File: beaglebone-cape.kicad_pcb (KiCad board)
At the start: 2 copper layers, 86.4 x 54.6 mm, 9 parts, among them J1 CONN_2X2, P1 BEAGLEBONE_BLACK, U1 24C16

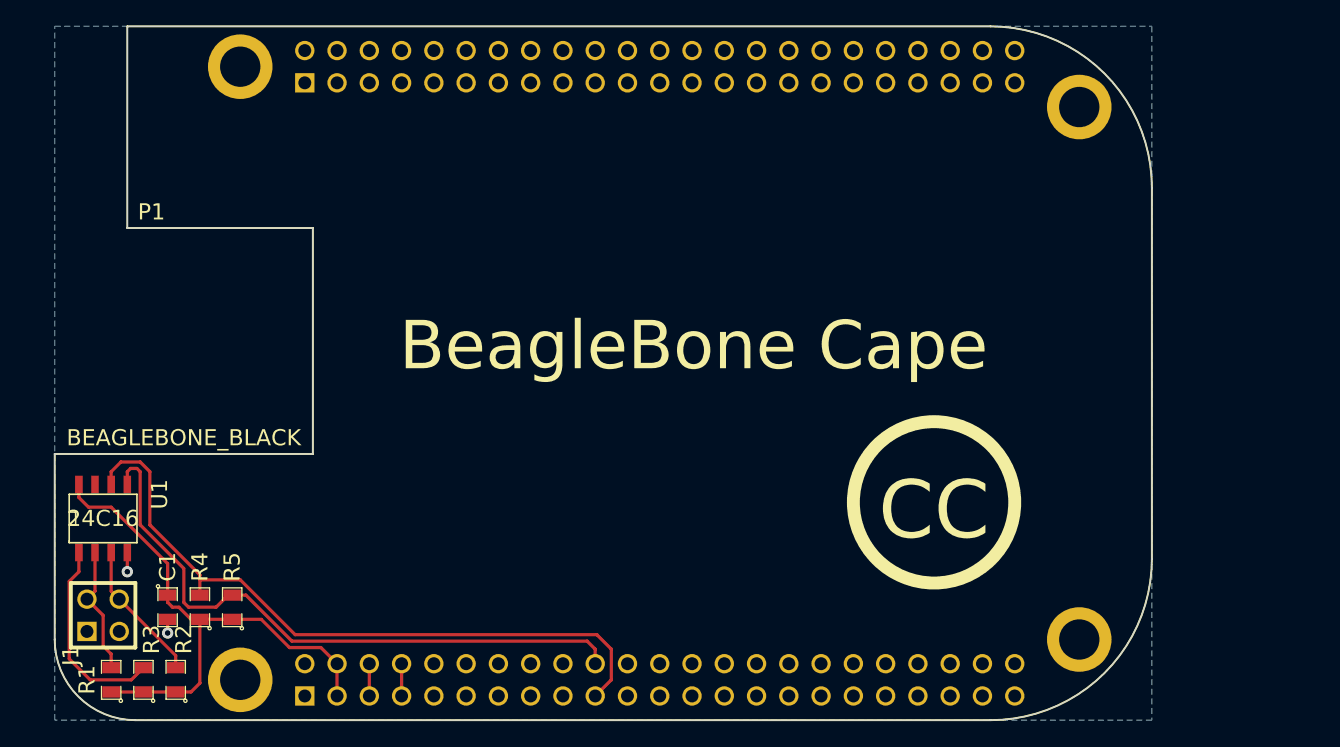
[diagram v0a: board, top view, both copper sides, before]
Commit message: Create the io cape base on the barebone cape
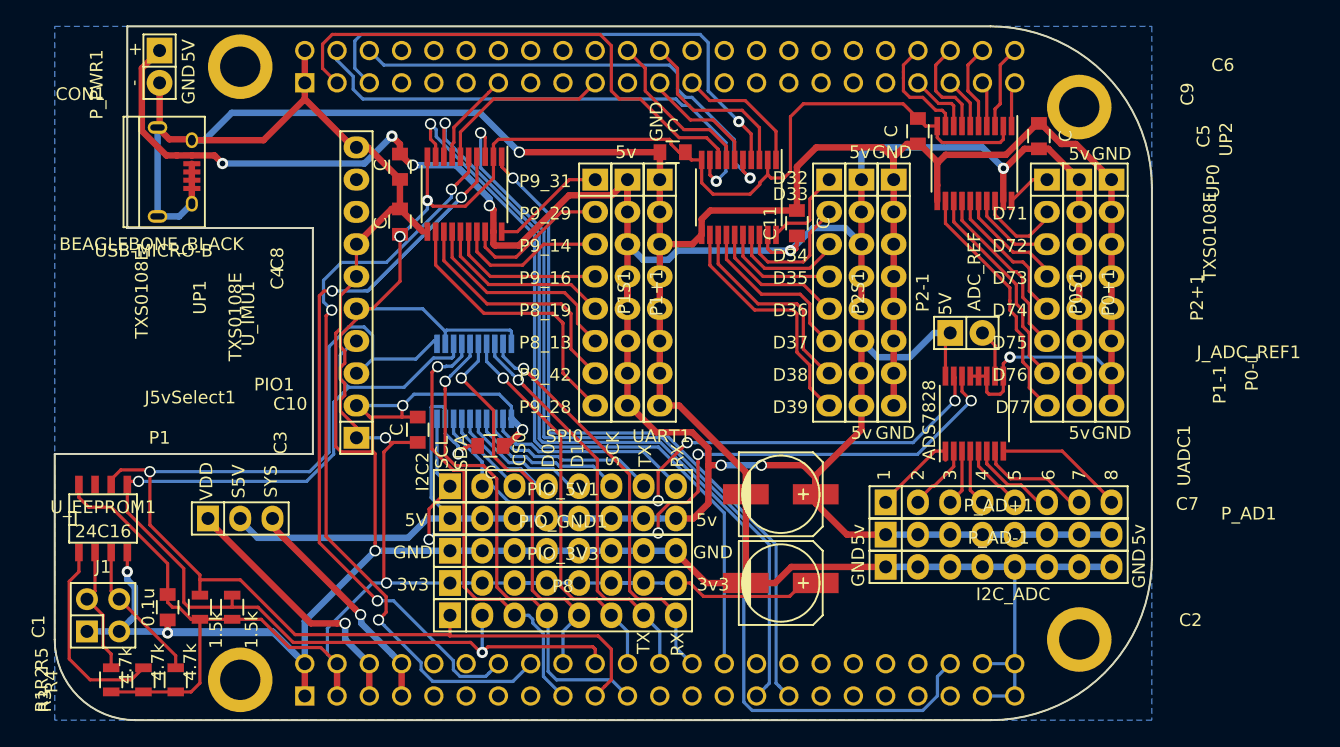
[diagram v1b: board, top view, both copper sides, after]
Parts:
- removed U1: 24C16, SO8E
- added C10: C, Capacitors_SMD:C_0805, F.Cu at (130.8, 118.1)
- added C11: C, Capacitors_SMD:C_0805, F.Cu at (154.9, 100.6)
- added C2: CP2, Capacitors_SMD:c_elec_6.3x5.7, F.Cu at (153.7, 128.9)
- added C3: C, Capacitors_SMD:C_0805, F.Cu at (125.1, 116.8)
- added C4: C, Capacitors_SMD:C_0805, F.Cu at (123.7, 100.5)
- added C5: C, Capacitors_SMD:C_0805, F.Cu at (164.5, 93.3)
- added C6: C, Capacitors_SMD:C_0805, F.Cu at (145.2, 95.0)
- added C7: CP2, Capacitors_SMD:c_elec_6.3x5.7, F.Cu at (153.7, 121.9)
- added C8: C, Capacitors_SMD:C_0805, F.Cu at (123.7, 96.1)
- added C9: C, Capacitors_SMD:C_0805, F.Cu at (174.0, 93.7)
- added CON1: USB-MICRO-B, Connect:USB_Micro-B, F.Cu at (107.3, 95.2)
- added J5vSelect1: CONN_01X03, Pin_Headers:Pin_Header_Straight_1x03, F.Cu at (111.1, 123.8)
- added J_ADC_REF1: CONN_01X02, Pin_Headers:Pin_Header_Straight_1x02, F.Cu at (168.3, 109.2)
- added P0+1: CONN_01X08, Pin_Headers:Pin_Header_Straight_1x08, F.Cu at (177.2, 106.0)
- added P0-1: CONN_01X08, Pin_Headers:Pin_Header_Straight_1x08, F.Cu at (179.7, 106.0)
- added P0S1: CONN_01X08, Pin_Headers:Pin_Header_Straight_1x08, F.Cu at (174.6, 106.0)
- added P1+1: CONN_01X08, Pin_Headers:Pin_Header_Straight_1x08, F.Cu at (141.6, 106.0)
- added P1-1: CONN_01X08, Pin_Headers:Pin_Header_Straight_1x08, F.Cu at (144.1, 106.0)
- added P1S1: CONN_01X08, Pin_Headers:Pin_Header_Straight_1x08, F.Cu at (139.1, 106.0)
- added P2+1: CONN_01X08, Pin_Headers:Pin_Header_Straight_1x08, F.Cu at (160.0, 106.0)
- added P2-1: CONN_01X08, Pin_Headers:Pin_Header_Straight_1x08, F.Cu at (162.6, 106.0)
- added P2S1: CONN_01X08, Pin_Headers:Pin_Header_Straight_1x08, F.Cu at (157.5, 106.0)
- added P8: CONN_01X08, Pin_Headers:Pin_Header_Straight_1x08, F.Cu at (136.5, 131.4)
- added PIO1: CONN_01X08, Pin_Headers:Pin_Header_Straight_1x08, F.Cu at (136.5, 121.3)
- added PIO_3V3: CONN_01X08, Pin_Headers:Pin_Header_Straight_1x08, F.Cu at (136.5, 128.9)
- added PIO_5V1: CONN_01X08, Pin_Headers:Pin_Header_Straight_1x08, F.Cu at (136.5, 123.8)
- added PIO_GND1: CONN_01X08, Pin_Headers:Pin_Header_Straight_1x08, F.Cu at (136.5, 126.4)
- added P_AD+1: CONN_01X08, Pin_Headers:Pin_Header_Straight_1x08, F.Cu at (170.8, 125.1)
- added P_AD-1: CONN_01X08, Pin_Headers:Pin_Header_Straight_1x08, F.Cu at (170.8, 127.6)
- added P_AD1: CONN_01X08, Pin_Headers:Pin_Header_Straight_1x08, F.Cu at (170.8, 122.6)
- added P_PWR1: CONN_01X02, Pin_Headers:Pin_Header_Straight_1x02, F.Cu at (104.8, 88.3)
- added UADC1: ADS7828, Housings_SSOP:TSSOP-16_4.4x5mm_Pitch0.65mm, F.Cu at (168.9, 115.6)
- added UP0: TXS0108E, Housings_SSOP:TSSOP-20_4.4x6.5mm_Pitch0.65mm, F.Cu at (168.9, 95.9)
- added UP1: TXS0108E, Housings_SSOP:TSSOP-20_4.4x6.5mm_Pitch0.65mm, F.Cu at (128.8, 98.3)
- added UP2: TXS0108E, Housings_SSOP:TSSOP-20_4.4x6.5mm_Pitch0.65mm, F.Cu at (150.4, 98.6)
- added UPIO1: TXS0108E, Housings_SSOP:TSSOP-20_4.4x6.5mm_Pitch0.65mm, B.Cu at (129.5, 113.0)
- added U_EEPROM1: 24C16, SMD_Packages:SOIC-8-W, F.Cu at (100.3, 123.8)
- added U_IMU1: BMX055-Breakout, Pin_Headers:Pin_Header_Straight_1x10, F.Cu at (120.3, 106.0)
- C1: footprint SM0805 -> Capacitors_SMD:C_0805
- J1: value CONN_2X2 -> CONN_02X02; footprint PIN_ARRAY_2X2 -> Pin_Headers:Pin_Header_Straight_2x02
- P1: footprint BEAGLEBONE_BLACK -> BeagleBoneBlack Cape:BEAGLEBONE_BLACK
- R1, R2, R3, R4, R5: footprint SM0805 -> Resistors_SMD:R_0805
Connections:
- P1 pad A10: (no net) -> /TIMER6
- P1 pad A11: (no net) -> /GPIO1_13
- P1 pad A12: (no net) -> /GPIO1_12
- P1 pad A13: (no net) -> /EHRPWM2B
- P1 pad A14: (no net) -> /GPIO0_26
- P1 pad A15: (no net) -> /GPIO1_15
- P1 pad A16: (no net) -> /GPIO1_14
- P1 pad A17: (no net) -> /GPIO0_27
- P1 pad A18: (no net) -> /GPIO2_1
- P1 pad A19: (no net) -> /EHRPWM2A
- P1 pad A20: (no net) -> /GPIO1_31
- P1 pad A21: (no net) -> /GPIO1_30
- P1 pad A22: (no net) -> /GPIO1_5
- P1 pad A23: (no net) -> /GPIO1_4
- P1 pad A24: (no net) -> /GPIO1_1
- P1 pad A25: (no net) -> /GPIO1_0
- P1 pad A26: (no net) -> /GPIO1_29
- P1 pad A27: (no net) -> /GPIO2_22
- P1 pad A28: (no net) -> /GPIO2_24
- P1 pad A29: (no net) -> /GPIO2_23
- P1 pad A3: (no net) -> /GPIO1_6
- P1 pad A30: (no net) -> /GPIO2_25
- P1 pad A31: (no net) -> /UART5_CTSN
- P1 pad A32: (no net) -> /UART5_RTSN
- P1 pad A33: (no net) -> /UART4_RTSN
- P1 pad A34: (no net) -> /UART3_RTSN
- P1 pad A35: (no net) -> /UART4_CTSN
- P1 pad A36: (no net) -> /UART3_CTSN
- P1 pad A37: (no net) -> /UART5_TXD
- P1 pad A38: (no net) -> /UART5_RXD
- P1 pad A39: (no net) -> /GPIO2_12
- P1 pad A4: (no net) -> /GPIO1_7
- P1 pad A40: (no net) -> /GPIO2_13
- P1 pad A41: (no net) -> /GPIO2_10
- P1 pad A42: (no net) -> /GPIO2_11
- P1 pad A43: (no net) -> /GPIO2_8
- P1 pad A44: (no net) -> /GPIO2_9
- P1 pad A45: (no net) -> /GPIO2_6
- P1 pad A46: (no net) -> /GPIO2_7
- P1 pad A5: (no net) -> /GPIO1_2
- P1 pad A6: (no net) -> /GPIO1_3
- P1 pad A7: (no net) -> /TIMER4
- P1 pad A8: (no net) -> /TIMER7
- P1 pad A9: (no net) -> /TIMER5
- P1 pad B10: (no net) -> /SYS_RESETn
- P1 pad B11: (no net) -> /UART4_RXD
- P1 pad B12: (no net) -> /GPIO1_28
- P1 pad B13: (no net) -> /UART4_TXD
- P1 pad B14: (no net) -> /EHRPWM1A
- P1 pad B15: (no net) -> /GPIO1_16
- P1 pad B16: (no net) -> /EHRPWM1B
- P1 pad B17: (no net) -> /I2C1_SCL
- P1 pad B18: (no net) -> /I2C1_SDA
- P1 pad B21: (no net) -> /SPI0_D0
- P1 pad B22: (no net) -> /SPI0_SCLK
- P1 pad B23: (no net) -> /GPIO1_17
- P1 pad B24: (no net) -> /UART1_TXD
- P1 pad B25: (no net) -> /GPIO3_21
- P1 pad B26: (no net) -> /UART1_RXD
- P1 pad B27: (no net) -> /GPIO3_19
- P1 pad B28: (no net) -> /ECAPPWM2
- P1 pad B29: (no net) -> /EHRPWM0B
- P1 pad B30: (no net) -> /SPI1_D1
- P1 pad B31: (no net) -> /EHRPWM0A
- P1 pad B32: (no net) -> /VADC
- P1 pad B33: (no net) -> /AIN4
- P1 pad B34: (no net) -> /AGND
- P1 pad B35: (no net) -> /AIN6
- P1 pad B36: (no net) -> /AIN5
- P1 pad B37: (no net) -> /AIN2
- P1 pad B38: (no net) -> /AIN3
- P1 pad B39: (no net) -> /AIN0
- P1 pad B40: (no net) -> /AIN1
- P1 pad B41: (no net) -> /CLKOUT2
- P1 pad B42: (no net) -> /ECAPPWM0
- P1 pad B9: (no net) -> /PWR_BUT
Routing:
- net GND: track 2.60 -> 526.9 mm, vias 2 -> 8
- net /SHLD_5V: track 0.00 -> 389.0 mm, vias 0 -> 9
- net /DC_3.3V: track 43.4 -> 214.5 mm, vias 0 -> 4
- net /ECAPPWM0: track 0.00 -> 82.3 mm, vias 0 -> 1
- net /EHRPWM1A: track 0.00 -> 67.2 mm, vias 0 -> 3
- net /P_I2C2_SCL: track 0.00 -> 62.6 mm, vias 0 -> 4
- net /EHRPWM0B: track 0.00 -> 61.6 mm, vias 0 -> 1
- net /EHRPWM1B: track 0.00 -> 60.8 mm, vias 0 -> 3
- net /ECAPPWM2: track 0.00 -> 60.2 mm, vias 0 -> 1
- net /EHRPWM0A: track 0.00 -> 57.1 mm, vias 0 -> 1
- net /P_I2C2_SDA: track 0.00 -> 52.0 mm, vias 0 -> 3
- net /GPIO1_2: track 0.00 -> 42.7 mm, vias 0 -> 1
- net /GPIO1_6: track 0.00 -> 41.6 mm
- net /GPIO1_7: track 0.00 -> 39.9 mm, vias 0 -> 1
- net /SPI0_D0: track 0.00 -> 39.4 mm, vias 0 -> 1
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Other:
- net class Default: clearance 0.2286 -> 0.1143
- net class Power added: clearance 0.1143, trace_width 0.508, via_dia 0.889, via_drill 0.635
- rule trace_clearance: 0.2286 -> 0.1143
- board text added: "+"
- board text added: "-"
- board text added: "1"
- board text added: "2"
- board text added: "3"
- board text added: "3v3"
- board text added: "4"
- board text added: "5"
- board text added: "5V"
- board text added: "5v"
- board text added: "6"
- board text added: "7"
- board text added: "8"
- board text added: "ADC_REF"
- board text added: "CS0"
- board text added: "D0"
- board text added: "D1"
- board text added: "D32"
- board text added: "D33"
- board text added: "D34"
- board text added: "D35"
- board text added: "D36"
- board text added: "D37"
- board text added: "D38"
- board text added: "D39"
- board text added: "D71"
- board text added: "D72"
- board text added: "D73"
- board text added: "D74"
- board text added: "D75"
- board text added: "D76"
- board text added: "D77"
- board text added: "GND"
- board text added: "I2C2"
- board text added: "I2C_ADC"
- board text added: "P8_13"
- board text added: "P8_19"
- board text added: "P9_14"
- board text added: "P9_16"
- board text added: "P9_28"
- board text added: "P9_29"
- board text added: "P9_31"
- board text added: "P9_42"
- board text added: "RX"
- board text added: "S5V"
- board text added: "SCK"
- board text added: "SCL"
- board text added: "SDA"
- board text added: "SPI0"
- board text added: "SYS"
- board text added: "TX"
- board text added: "UART1"
- board text added: "VDD"
- board text removed: "BeagleBone Cape"
- board text removed: "CC"
